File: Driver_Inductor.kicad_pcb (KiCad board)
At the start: 6 copper layers, 120.5 x 72.9 mm, 99 parts, among them J1 2-338069-0, J2 DC+, J3 DC-, J4 OUT1, J5 OUT2, U1 R-783.3-1.0, U2 R-785.0-1.0, U3 LM1117GS-3.3, U4 LMV331, U5 ADuM1200AR, U6 74LVC1G04

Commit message: Тестовая версия
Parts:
- removed C29: 2.2u, Capacitor_SMD:C_0805_2012Metric_Pad1.18x1.45mm_HandSolder
- removed D18: ADM3485E, Package_SO:SOIC-8_3.9x4.9mm_P1.27mm
- removed R24: 120, Resistor_SMD:R_0805_2012Metric_Pad1.20x1.40mm_HandSolder
- C11, C12, C13, C14, C37, D3, D4, R31, U6: moved to B.Cu
- J2, J3: footprint Connector Power:M4 -> Connector_Power:M5
- J4, J5: footprint Connector Power:M5 -> Connector_Power:M5
- R10, R30, R9: moved to F.Cu
- moved D5 68.7 mm to (113.0, 93.3)
- moved U6 49.2 mm to (149.5, 86.3), turned to 180 degrees
- moved R31 47.6 mm to (154.6, 86.3), turned to -90 degrees
- moved R30 47.2 mm to (157.1, 86.2), turned to -90 degrees
- moved C37 47.2 mm to (157.1, 86.3), turned to -90 degrees
- moved C22 45.1 mm to (181.0, 123.4)
- moved U2 45.1 mm to (176.0, 127.3)
- moved C20 45.1 mm to (175.3, 123.4)
- moved C18 38.6 mm to (129.7, 124.3), turned to 0 degrees
- moved C17 36.9 mm to (137.2, 125.6), turned to 180 degrees
- moved R9 36.7 mm to (113.0, 101.5), turned to -90 degrees
- moved D15 30.0 mm to (121.9, 127.2), turned to 180 degrees
- moved D16 25.5 mm to (145.0, 122.8), turned to 0 degrees
- moved C15 24.1 mm to (157.1, 110.5)
- moved D13 24.1 mm to (150.7, 110.5)
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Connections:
- C25 pad 2: E1 -> E3
- C26 pad 1: E1 -> E3
- C28 pad 1: Net-(C28-Pad1) -> Current
- C30 pad 1: E1 -> E3
- D16 pad 7: E1 -> E3
- D17 pad 1: E3 -> OUT2
- D17 pad 12: Net-(C28-Pad1) -> Current
- D17 pad 2: E3 -> OUT2
- D17 pad 3: E3 -> OUT2
- D17 pad 4: E3 -> OUT2
- D17 pad 5: OUT+ -> OUT2_Sens
- D17 pad 6: OUT+ -> OUT2_Sens
- D17 pad 7: OUT+ -> OUT2_Sens
- D17 pad 8: OUT+ -> OUT2_Sens
- D20 pad 15: DESAT_H -> unconnected-(D20-Pad15)
- D20 pad 21: E3 -> OUT2
- D20 pad 22: E3 -> OUT2
- D20 pad 23: E1 -> OUT1
- D20 pad 24: E1 -> OUT1
- D20 pad 25: Net-(D20-Pad25) -> DESAT_H
- D20 pad 26: Net-(D20-Pad25) -> DESAT_H
- D7 pad 1: E1 -> OUT1
- J1 pad 1: GND -> Fault_N
- J1 pad 10: Fault_N -> +15V
- J1 pad 11: Temp_P -> Temp_N
- J1 pad 12: Temp_N -> Temp_P
- J1 pad 13: PWM2_P -> PWM1_P
- J1 pad 14: PWM2_N -> PWM1_N
- J1 pad 15: PWM1_P -> PWM2_P
- J1 pad 16: PWM1_N -> PWM2_N
- J1 pad 18: +15V -> Reset
- J1 pad 2: +15V -> Fault_P
- J1 pad 20: Reset -> Current
- J1 pad 7: Current_P -> GND
- J1 pad 8: Current_N -> +15V
- J1 pad 9: Fault_P -> GND
- J2 pad 1: Net-(D20-Pad25) -> DESAT_H
- J4 pad 1: E1 -> OUT1
- J5 pad 1: E3 -> OUT2_Sens
- U3 pad 3: E1 -> E3
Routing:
- net RST_H1: track 103.4 -> 33.5 mm
- net E3: track 8.36 -> 70.5 mm
- net PWM1_N: track 78.6 -> 28.7 mm
- net PWM1_P: track 71.4 -> 22.9 mm
- net PWM2_N: track 87.4 -> 42.1 mm
- net PWM2_P: track 80.5 -> 36.2 mm
- net Net-(D5-Pad2): track 41.7 -> 3.73 mm, vias 1 -> 0
- net Current_N: track 37.2 -> 0.00 mm, vias 2 -> 0
- net Current_P: track 33.5 -> 0.00 mm, vias 2 -> 0
- net -15V_H1: track 51.3 -> 20.1 mm, vias 7 -> 8
- net Net-(D13-Pad8): track 14.2 -> 43.0 mm
- net Net-(C5-Pad1): track 14.1 -> 37.9 mm
- net Current: track 0.00 -> 22.8 mm, vias 0 -> 2
- net Fault_P: track 28.2 -> 6.33 mm, vias 2 -> 0
- net Fault_N: track 31.9 -> 11.1 mm, vias 2 -> 0
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- added copper zone on In1.Cu, net +15V
- added copper zone on In3.Cu, net +15V_H1
- added copper zone on In3.Cu, net +15V_L1
- added copper zone on In3.Cu, net +3.3VA
- added copper zone on In3.Cu, net +3V3
- added copper zone on In4.Cu, net -15V_H1
- added copper zone on In4.Cu, net -15V_L1
- added copper zone on B.Cu, net DESAT_H
- added copper zone on F.Cu, net DESAT_H
- added copper zone on B.Cu, net E3
- added copper zone on In2.Cu, net GND
- added copper zone on B.Cu, net Net-(D20-Pad27)
- added copper zone on F.Cu, net Net-(D20-Pad27)
- added copper zone on B.Cu, net OUT1
- added copper zone on F.Cu, net OUT1
- added copper zone on In1.Cu, net OUT1
- added copper zone on In2.Cu, net OUT1
- added copper zone on B.Cu, net OUT2
- added copper zone on In3.Cu, net OUT2
- added copper zone on In4.Cu, net OUT2
- added copper zone on B.Cu, net OUT2_Sens
- added copper zone on In3.Cu, net OUT2_Sens
- added copper zone on In4.Cu, net OUT2_Sens
- removed copper zone on In2.Cu, net +15V
- removed copper zone on In1.Cu, net +15V_H1
- removed copper zone on In1.Cu, net +15V_L1
- removed copper zone on B.Cu, net -15V_H1
- removed copper zone on In2.Cu, net -15V_H1
- removed copper zone on In2.Cu, net -15V_L1
- removed copper zone on In1.Cu, net DESAT_H
- removed copper zone on In2.Cu, net DESAT_H
- removed copper zone on B.Cu, net E1
- removed copper zone on In3.Cu, net E1
- removed copper zone on In1.Cu, net E2
- removed copper zone on In4.Cu, net E3
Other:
- board size 120.5 x 72.9 mm -> 120.6 x 69.9 mm
- board text added: "DC+"
- board text added: "DC-"
- board text added: "Driver GD50FFY120C5S VER1.0.TEST"
- board text added: "FLT"
- board text added: "OUT+"
- board text added: "OUT-"
- board text added: "RDY"

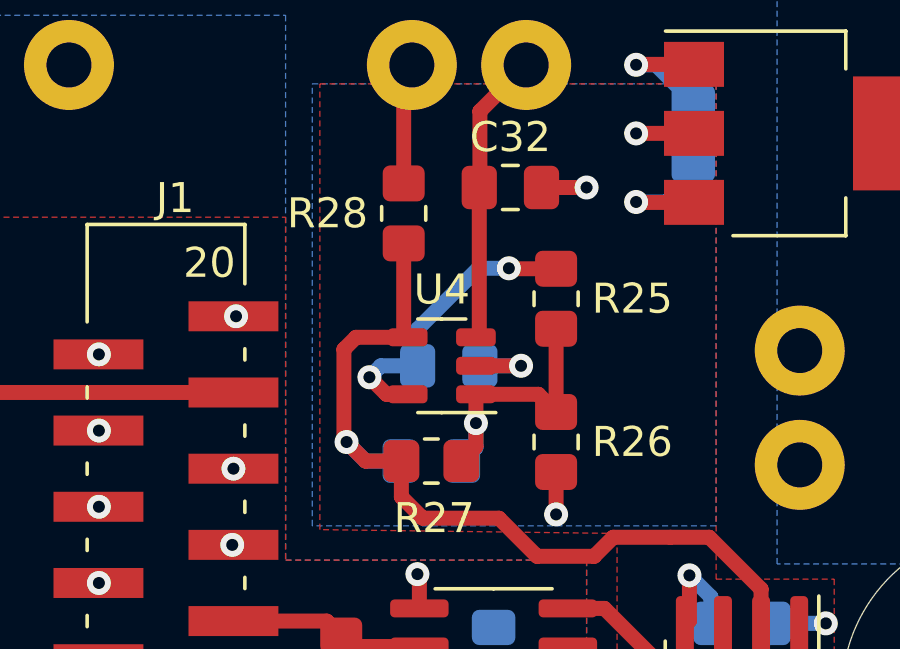
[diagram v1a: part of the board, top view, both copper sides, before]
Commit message: Заменил компаратор на пушпульный
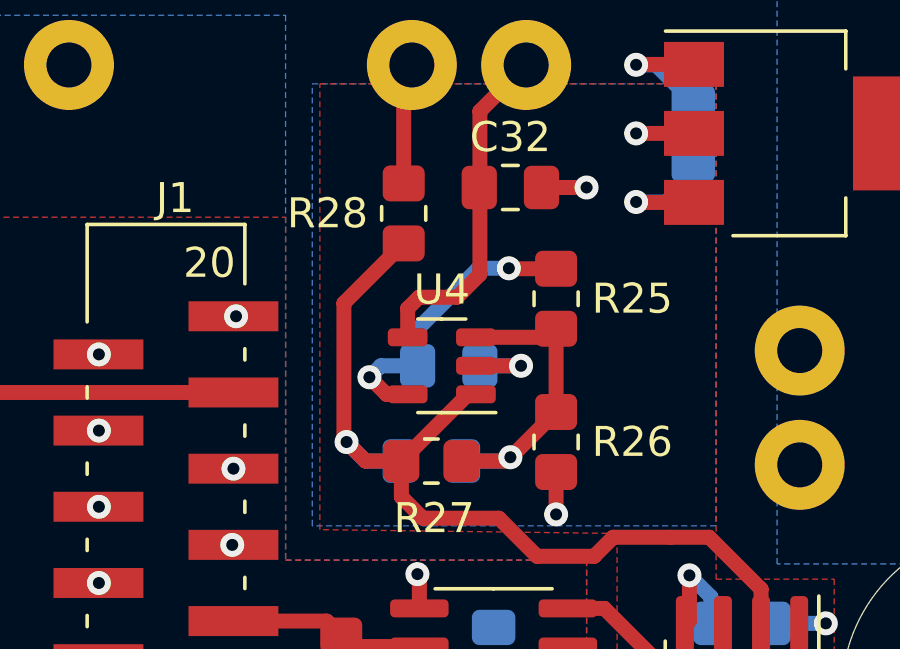
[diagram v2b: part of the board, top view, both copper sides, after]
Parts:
- R7, R8: value 1.1k -> 10k
- U4: value LMV331 -> LMV7219M5
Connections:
- C33 pad 1: Net-(C33-Pad1) -> Net-(U4-+)
- C33 pad 2: Net-(C33-Pad2) -> Net-(U5-VIA)
- R25 pad 1: Net-(C33-Pad1) -> Net-(U4-+)
- R26 pad 2: Net-(C33-Pad1) -> Net-(U4-+)
- R27 pad 1: Net-(C33-Pad1) -> Net-(U4-+)
- R27 pad 2: Net-(C33-Pad2) -> Net-(U5-VIA)
- R28 pad 1: Net-(C33-Pad2) -> Net-(U5-VIA)
- U4 pad 1: Net-(C33-Pad1) -> Net-(U5-VIA)
- U4 pad 3: NTC1 -> Net-(U4-+)
- U4 pad 4: Net-(C33-Pad2) -> NTC1
- U5 pad 2: Net-(C33-Pad2) -> Net-(U5-VIA)
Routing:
- net Net-(U5-VIA): track 0.00 -> 31.3 mm, vias 0 -> 1
- net Net-(C33-Pad2): track 28.7 -> 0.00 mm, vias 1 -> 0
- net Net-(U4-+): track 0.00 -> 11.1 mm, vias 0 -> 1
- net Net-(C33-Pad1): track 9.57 -> 0.00 mm, vias 1 -> 0
- net NTC1: track 9.59 -> 11.3 mm

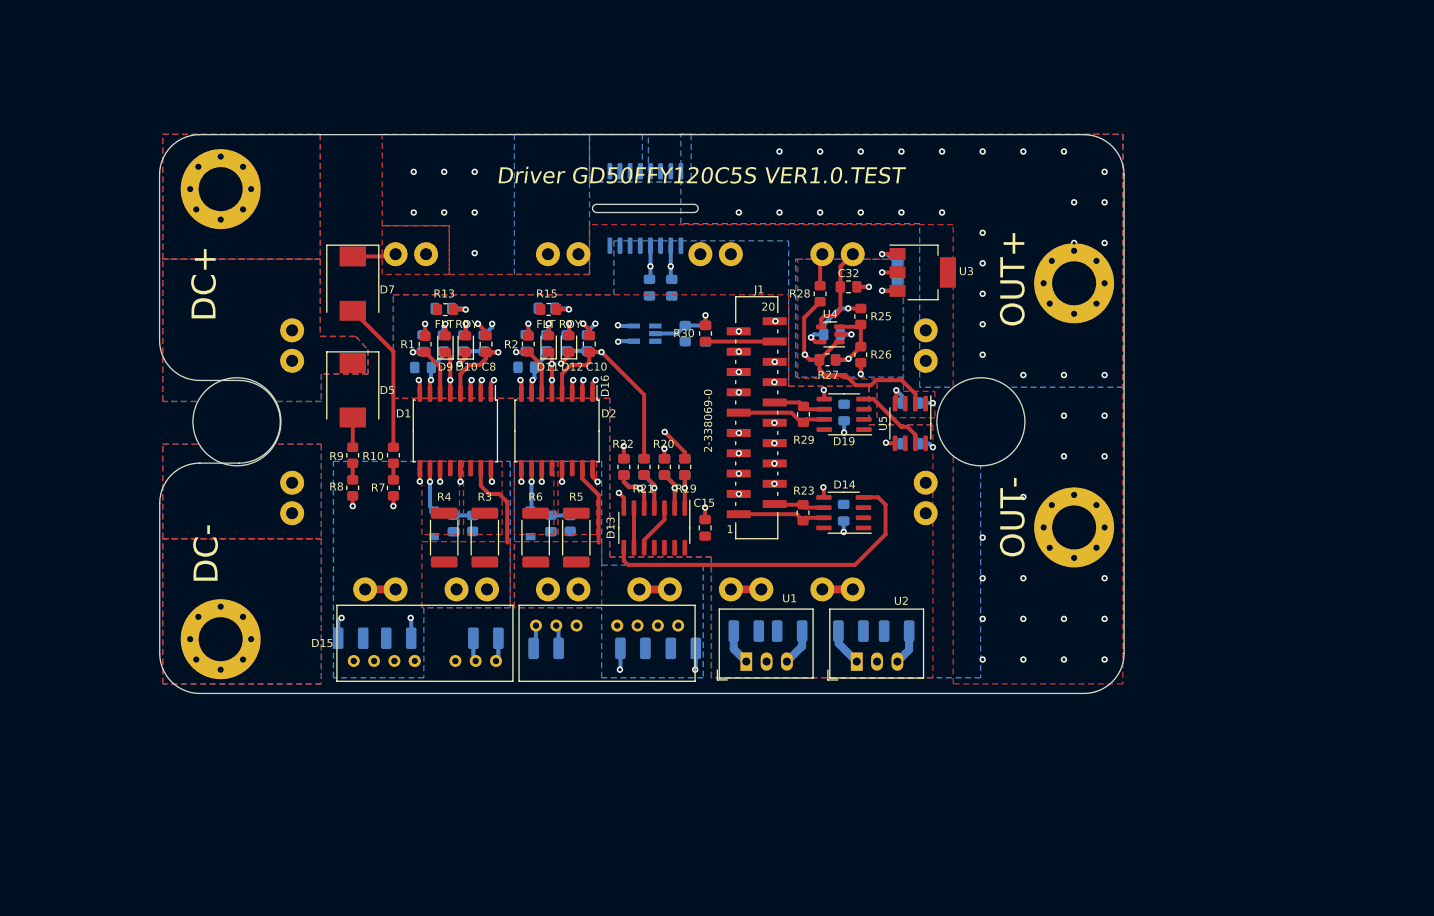
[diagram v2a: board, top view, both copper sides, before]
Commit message: Убрал питание 3.3В
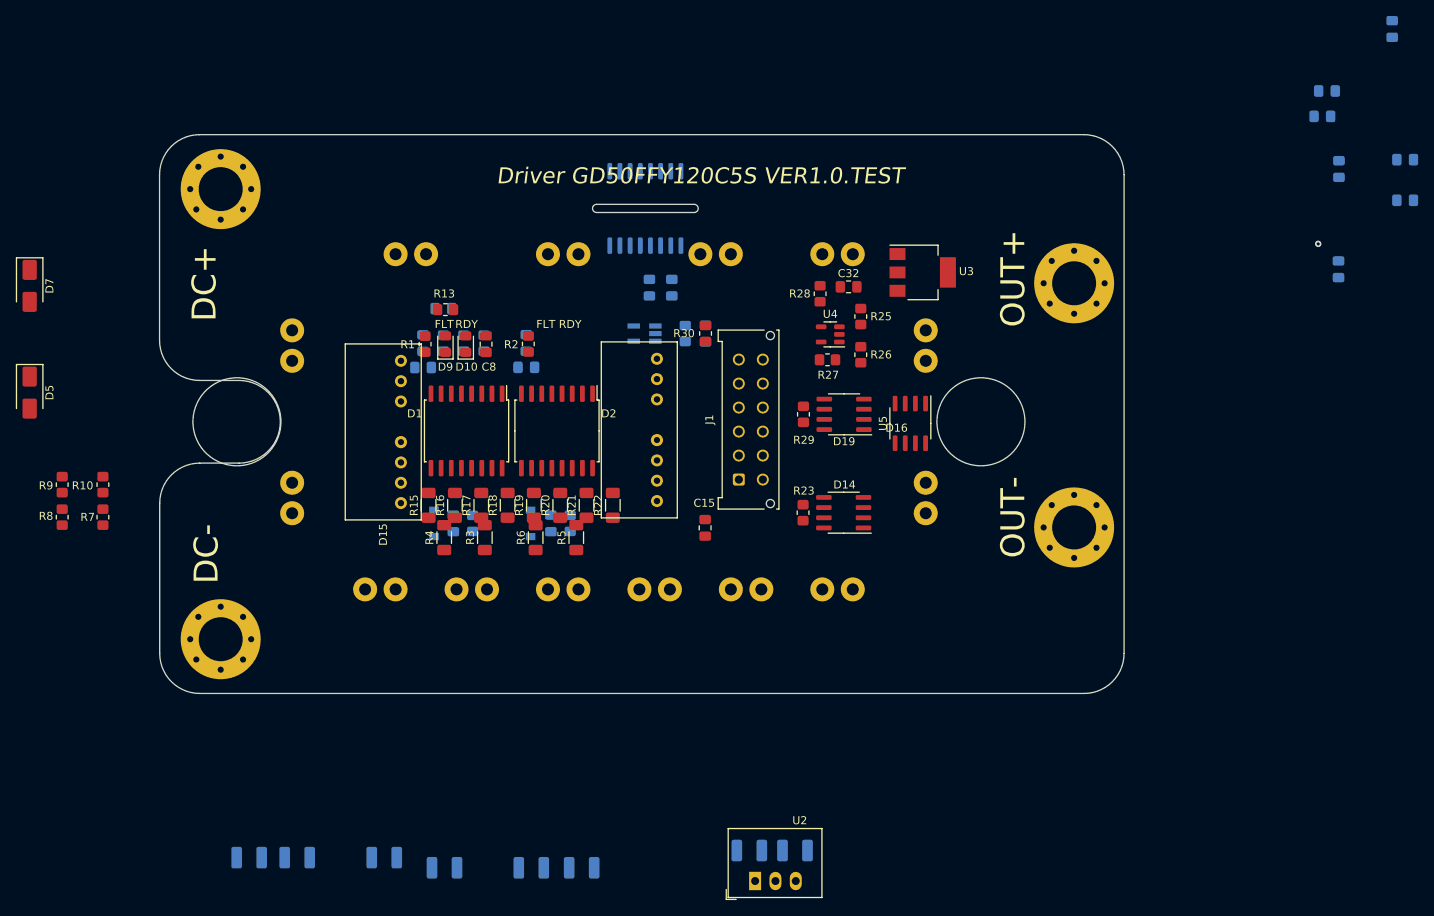
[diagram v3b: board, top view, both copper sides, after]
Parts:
- removed C10, C11, C12, C13, C14, C9: 56p, Capacitor_SMD:C_0805_2012Metric_Pad1.18x1.45mm_HandSolder
- removed C19, C21: 10u, Capacitor_SMD:C_1210_3225Metric_Pad1.33x2.70mm_HandSolder
- removed D11: FLT, LED_SMD:LED_0805_2012Metric_Pad1.15x1.40mm_HandSolder
- removed D12: RDY, LED_SMD:LED_0805_2012Metric_Pad1.15x1.40mm_HandSolder
- removed D13: SN74AC08DR, Package_SO:SOIC-14_3.9x8.7mm_P1.27mm
- removed U1: R-783.3-1.0, Converter_DCDC:Converter_DCDC_RECOM_R-78E-0.5_THT
- D5, D7: footprint Diode_SMD:D_SMC -> Diode_SMD:D_SMA
- J1: value 2-338069-0 -> Control_A; footprint Connector_My:2-338069-0 -> Connector_Molex:Molex_Micro-Fit_3.0_43045-1212_2x06_P3.00mm_Vertical
- R15: value 10k -> 10; footprint Resistor_SMD:R_0805_2012Metric_Pad1.20x1.40mm_HandSolder -> Resistor_SMD:R_1206_3216Metric_Pad1.30x1.75mm_HandSolder
- R16, R18: value 330 -> 10; footprint Resistor_SMD:R_0805_2012Metric_Pad1.20x1.40mm_HandSolder -> Resistor_SMD:R_1206_3216Metric_Pad1.30x1.75mm_HandSolder; moved to F.Cu
- R17: value 120 -> 10; footprint Resistor_SMD:R_0805_2012Metric_Pad1.20x1.40mm_HandSolder -> Resistor_SMD:R_1206_3216Metric_Pad1.30x1.75mm_HandSolder; moved to F.Cu
- R19, R20, R21, R22: value 120 -> 10; footprint Resistor_SMD:R_0805_2012Metric_Pad1.20x1.40mm_HandSolder -> Resistor_SMD:R_1206_3216Metric_Pad1.30x1.75mm_HandSolder
- R3, R4, R5, R6: value 3.9 -> 10; footprint Resistor_SMD:R_2512_6332Metric_Pad1.40x3.35mm_HandSolder -> Resistor_SMD:R_1206_3216Metric_Pad1.30x1.75mm_HandSolder
- moved C16 68.9 mm to (236.2, 78.2)
- moved C30 68.9 mm to (243.0, 48.2)
- moved C31 68.9 mm to (234.8, 55.9)
- moved C33 68.9 mm to (234.2, 59.1)
- moved C34 68.9 mm to (244.6, 64.5)
- moved C35 68.9 mm to (244.6, 69.6)
- moved C36 68.9 mm to (236.3, 65.7)
- moved D5 40.4 mm to (72.6, 93.6)
- moved D7 40.4 mm to (72.6, 80.3)
- moved R10 36.5 mm to (81.8, 105.1)
- moved R7 36.5 mm to (81.8, 109.2)
- moved R8 36.5 mm to (76.7, 109.2)
- moved R9 36.5 mm to (76.7, 105.1)
- moved C18 30.2 mm to (117.0, 151.8)
- moved C23 30.2 mm to (106.1, 151.8)
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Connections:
- net +3.3VA renamed +5VP
- net RST_H1 renamed RST
- C1 pad 2: +3V3 -> +5V
- C15 pad 1: +3V3 -> +5V
- C16 pad 1: +3V3 -> +5V
- C2 pad 2: +3V3 -> +5V
- C30 pad 1: E3 -> E2
- C30 pad 2: -15V_H1 -> -15V_L1
- C31 pad 2: -15V_H1 -> -15V_L1
- C32 pad 2: -15V_H1 -> -15V_L1
- C34 pad 2: -15V_H1 -> -15V_L1
- C35 pad 1: +3V3 -> +5V
- C36 pad 1: +3V3 -> +5V
- C7 pad 1: FLT_L1 -> FLT
- C8 pad 1: RDY_L1 -> RDY
- D1 pad 4: RDY_L1 -> RDY
- D1 pad 5: FLT_L1 -> FLT
- D1 pad 7: +3V3 -> +5V
- D14 pad 2: +3V3 -> +5V
- D14 pad 3: +3V3 -> +5V
- D14 pad 8: +3V3 -> +5V
- D19 pad 2: +3V3 -> +5V
- D19 pad 3: +3V3 -> +5V
- D19 pad 8: +3V3 -> +5V
- D2 pad 4: RDY_H1 -> RDY
- D2 pad 5: FLT_H1 -> FLT
- D2 pad 7: +3V3 -> +5V
- D9 pad 1: FLT_L1 -> FLT
- J1 pad 1: Fault_N -> unconnected-(J1-Pin_1-Pad1)
- J1 pad 10: +15V -> unconnected-(J1-Pin_10-Pad10)
- J1 pad 11: Temp_N -> unconnected-(J1-Pin_11-Pad11)
- J1 pad 12: Temp_P -> unconnected-(J1-Pin_12-Pad12)
- J1 pad 2: Fault_P -> unconnected-(J1-Pin_2-Pad2)
- J1 pad 3: GND -> unconnected-(J1-Pin_3-Pad3)
- J1 pad 4: +15V -> unconnected-(J1-Pin_4-Pad4)
- J1 pad 5: GND -> unconnected-(J1-Pin_5-Pad5)
- J1 pad 6: +15V -> unconnected-(J1-Pin_6-Pad6)
- J1 pad 7: GND -> unconnected-(J1-Pin_7-Pad7)
- J1 pad 8: +15V -> unconnected-(J1-Pin_8-Pad8)
- J1 pad 9: GND -> unconnected-(J1-Pin_9-Pad9)
- R11 pad 2: +3V3 -> +5V
- R12 pad 2: RDY_L1 -> RDY
- R13 pad 1: FLT_L1 -> FLT
- R13 pad 2: +3V3 -> unconnected-(R13-Pad2)
- R14 pad 1: RDY_L1 -> RDY
- R14 pad 2: +3V3 -> +5V
- R15 pad 1: FLT_H1 -> G2
- R15 pad 2: +3V3 -> Net-(D1-Vout_on)
- R16 pad 1: Net-(D11-A) -> G2
- R16 pad 2: +3V3 -> Net-(D1-Vout_on)
- R17 pad 1: RDY_H1 -> G2
- R17 pad 2: +3V3 -> Net-(D1-Vout_off)
- R18 pad 1: Net-(D12-A) -> G2
- R18 pad 2: RDY_H1 -> Net-(D1-Vout_off)
- R19 pad 1: Net-(D13-1A) -> G3
- R19 pad 2: FLT_H1 -> Net-(D2-Vout_on)
- R20 pad 1: Net-(D13-1B) -> G3
- R20 pad 2: FLT_L1 -> Net-(D2-Vout_off)
- R21 pad 1: Net-(D13-2A) -> G3
- R21 pad 2: RDY_H1 -> Net-(D2-Vout_off)
- R22 pad 1: Net-(D13-2B) -> G3
- R22 pad 2: RDY_L1 -> Net-(D2-Vout_off)
- R26 pad 1: -15V_H1 -> -15V_L1
- R6 pad 2: Net-(D2-Vout_off) -> Net-(D2-Vout_on)
- U3 pad 1: -15V_H1 -> -15V_L1
- U3 pad 3: E3 -> E2
- U4 pad 2: -15V_H1 -> -15V_L1
- U5 pad 4: -15V_H1 -> -15V_L1
- U5 pad 8: +3V3 -> +5V
- U6 pad 5: +3V3 -> +5V
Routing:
- net +5V: track 74.9 -> 0.00 mm, vias 1 -> 0
- net E3: track 70.5 -> 0.00 mm, vias 2 -> 0
- net FLT_L1: track 50.7 -> 0.00 mm, vias 3 -> 0
- net RDY_L1: track 47.0 -> 0.00 mm, vias 2 -> 0
- net Net-(D14-DI): track 43.0 -> 0.00 mm
- net PWM2_N: track 42.1 -> 0.00 mm, vias 2 -> 0
- net Net-(D2-DESAT): track 37.9 -> 0.00 mm, vias 2 -> 0
- net FLT_H1: track 37.7 -> 0.00 mm, vias 4 -> 0
- net PWM2_P: track 36.2 -> 0.00 mm, vias 2 -> 0
- net RST: track 33.5 -> 0.00 mm, vias 3 -> 0
- net Net-(U5-VIA): track 31.3 -> 0.00 mm, vias 1 -> 0
- net RDY_H1: track 29.2 -> 0.00 mm, vias 1 -> 0
- net PWM1_N: track 28.7 -> 0.00 mm, vias 2 -> 0
- net GND: track 27.4 -> 0.00 mm, vias 19 -> 1
- net +3V3: track 27.2 -> 0.00 mm, vias 8 -> 0
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- removed copper zone on In1.Cu, net +15V
- removed copper zone on In3.Cu, net +15V_H1
- removed copper zone on In3.Cu, net +15V_L1
- removed copper zone on F.Cu, net +3V3
- removed copper zone on In3.Cu, net +3V3
- removed copper zone on F.Cu, net +5VP
- removed copper zone on In3.Cu, net +5VP
- removed copper zone on In4.Cu, net -15V_H1
- removed copper zone on In4.Cu, net -15V_L1
- removed copper zone on B.Cu, net DESAT_H
- removed copper zone on F.Cu, net DESAT_H
- removed copper zone on B.Cu, net E2
- removed copper zone on B.Cu, net E3
- removed copper zone on F.Cu, net G2
- removed copper zone on F.Cu, net G3
- removed copper zone on B.Cu, net GND
- removed copper zone on In2.Cu, net GND
- removed copper zone on F.Cu, net Net-(D1-Vout_off)
- removed copper zone on F.Cu, net Net-(D1-Vout_on)
- removed copper zone on F.Cu, net Net-(D2-Vout_off)
- removed copper zone on F.Cu, net Net-(D2-Vout_on)
- removed copper zone on B.Cu, net Net-(J3-Pin_1)
- removed copper zone on F.Cu, net Net-(J3-Pin_1)
- removed copper zone on B.Cu, net OUT1
- removed copper zone on F.Cu, net OUT1
- removed copper zone on In1.Cu, net OUT1
- removed copper zone on In2.Cu, net OUT1
- removed copper zone on B.Cu, net OUT2
- removed copper zone on In3.Cu, net OUT2
- removed copper zone on In4.Cu, net OUT2
- removed copper zone on B.Cu, net OUT2_Sens
- removed copper zone on In3.Cu, net OUT2_Sens
- removed copper zone on In4.Cu, net OUT2_Sens
